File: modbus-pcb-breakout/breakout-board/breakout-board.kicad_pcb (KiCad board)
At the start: 2 copper layers, 25 parts, among them J1 Screw_Terminal_01x02, J10 Screw_Terminal_01x02, J11 Screw_Terminal_01x02, J12 Screw_Terminal_01x02, J13 Screw_Terminal_01x02, J14 Screw_Terminal_01x02, J15 Screw_Terminal_01x02, J16 Screw_Terminal_01x02, J17 Screw_Terminal_01x02, J2 Screw_Terminal_01x02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

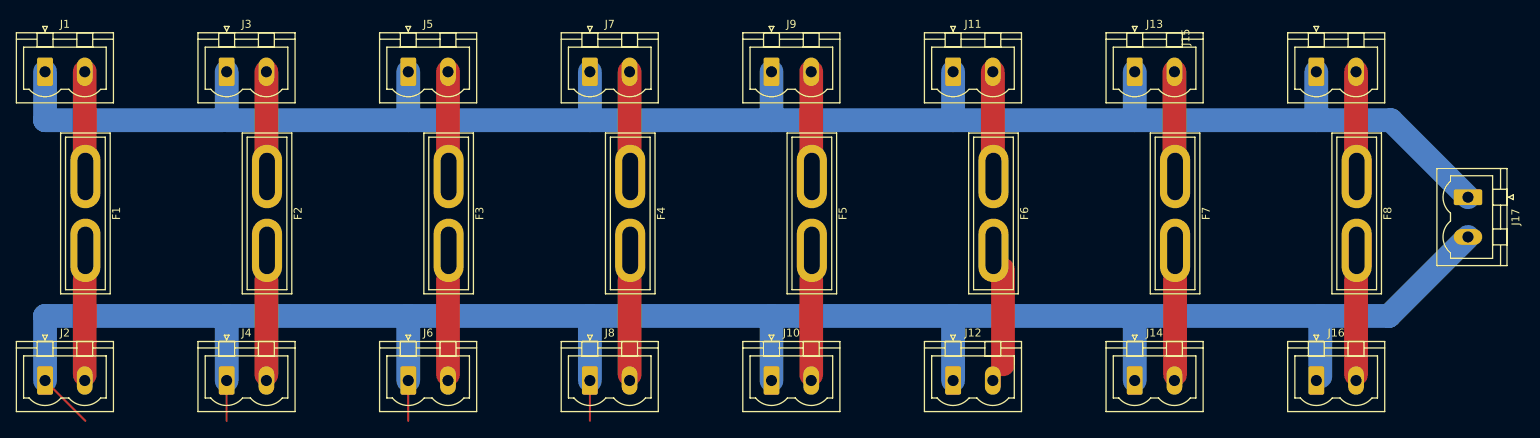
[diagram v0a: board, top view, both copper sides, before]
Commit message: Updating fuse positions
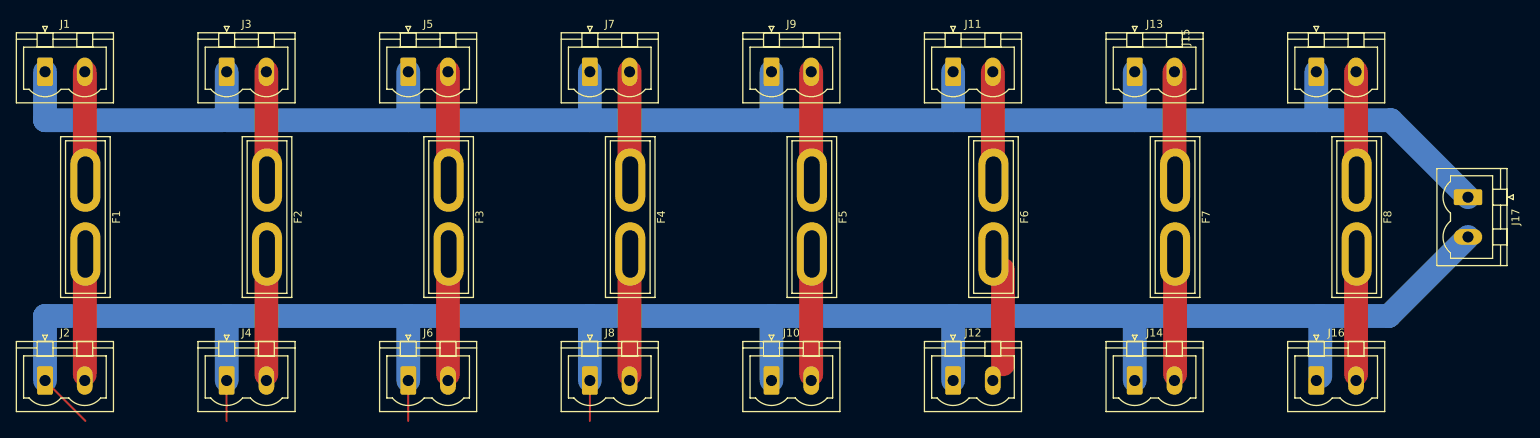
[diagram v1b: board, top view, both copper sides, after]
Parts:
- moved F1 0.46 mm to (50.8, 51.7)
- moved F2 0.46 mm to (73.7, 51.7)
- moved F3 0.46 mm to (96.5, 51.7)
- moved F4 0.46 mm to (119.4, 51.7)
- moved F5 0.46 mm to (142.2, 51.7)
- moved F6 0.46 mm to (165.1, 51.7)
- moved F7 0.46 mm to (188.0, 51.7)
- moved F8 0.46 mm to (210.8, 51.7)
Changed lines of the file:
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@@
   )
   (footprint "Fuse:Fuse_Blade_ATO_directSolder" (layer "F.Cu")
-    (at 96.52 51.28 -90)
+    (at 96.52 51.738 -90)
     (descr "car blade fuse direct solder")
     (tags "car blade fuse")
@@
   )
   (footprint "Fuse:Fuse_Blade_ATO_directSolder" (layer "F.Cu")
-    (at 73.66 51.28 -90)
+    (at 73.66 51.738 -90)
     (descr "car blade fuse direct solder")
     (tags "car blade fuse")
@@
   )
   (footprint "Fuse:Fuse_Blade_ATO_directSolder" (layer "F.Cu")
-    (at 50.8 51.28 -90)
+    (at 50.8 51.738 -90)
     (descr "car blade fuse direct solder")
     (tags "car blade fuse")
@@
   )
   (footprint "Fuse:Fuse_Blade_ATO_directSolder" (layer "F.Cu")
-    (at 187.96 51.28 -90)
+    (at 187.96 51.738 -90)
     (descr "car blade fuse direct solder")
     (tags "car blade fuse")
@@
   )
   (footprint "Fuse:Fuse_Blade_ATO_directSolder" (layer "F.Cu")
-    (at 119.38 51.28 -90)
+    (at 119.38 51.738 -90)
     (descr "car blade fuse direct solder")
     (tags "car blade fuse")
@@
   )
   (footprint "Fuse:Fuse_Blade_ATO_directSolder" (layer "F.Cu")
-    (at 165.1 51.28 -90)
+    (at 165.1 51.738 -90)
     (descr "car blade fuse direct solder")
     (tags "car blade fuse")
@@
   )
   (footprint "Fuse:Fuse_Blade_ATO_directSolder" (layer "F.Cu")
-    (at 142.24 51.28 -90)
+    (at 142.24 51.738 -90)
     (descr "car blade fuse direct solder")
     (tags "car blade fuse")
@@
   )
   (footprint "Fuse:Fuse_Blade_ATO_directSolder" (layer "F.Cu")
-    (at 210.82 51.28 -90)
+    (at 210.82 51.738 -90)
     (descr "car blade fuse direct solder")
     (tags "car blade fuse")
